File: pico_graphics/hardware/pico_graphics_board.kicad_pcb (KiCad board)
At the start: 2 copper layers, 99.1 x 86.4 mm, 28 parts, among them J1 8bit_thing_bus_connector, J2 HDMI_A, J3 greenpak_i2c, U1 Pico, U2 74LVC245, U3 74LVC245, U4 SLG46826G

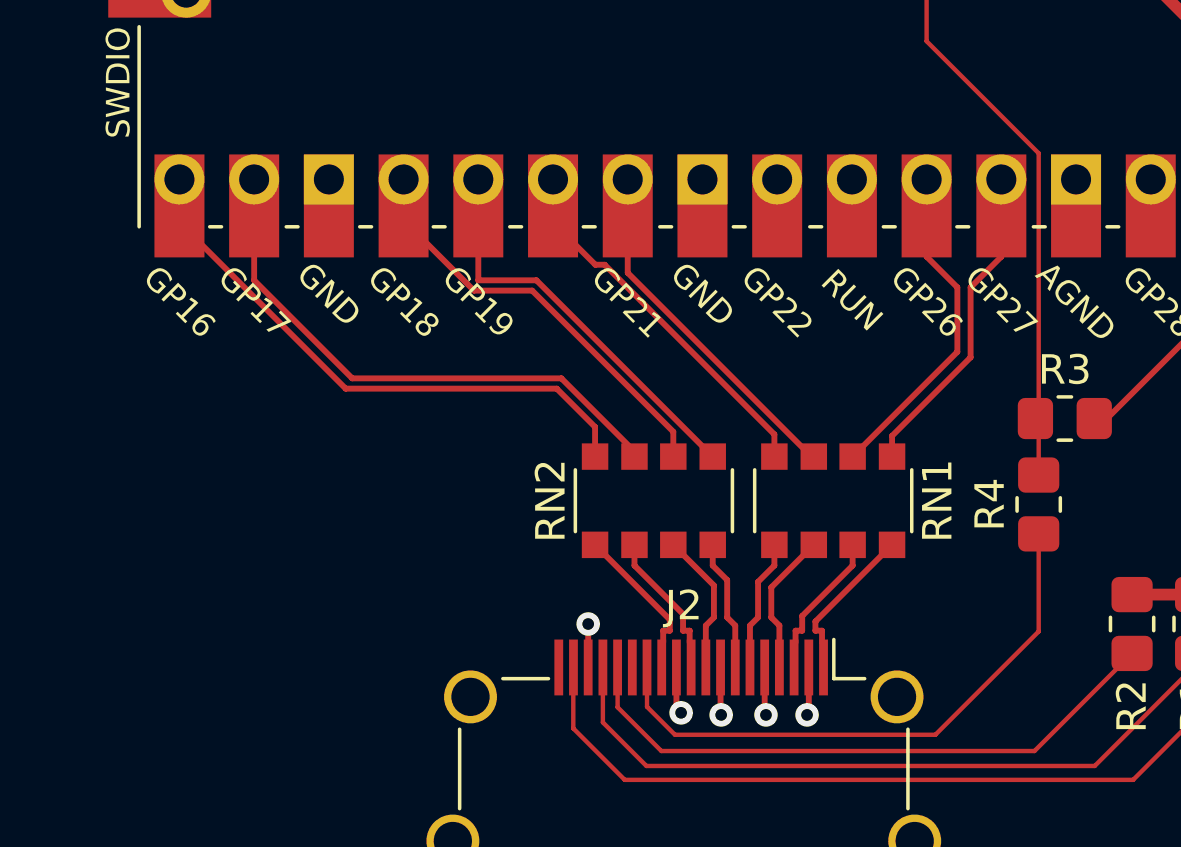
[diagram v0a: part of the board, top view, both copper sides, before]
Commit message: Fix resistor network footprint size
Kicad footprints are confusingly labeled by the individual resistor size as
opposed to the size of the full package - so 4x1206 means 'as big as 4x 1206
resistors' not as big as one 1206 as is used in manufacturers' datasheets.
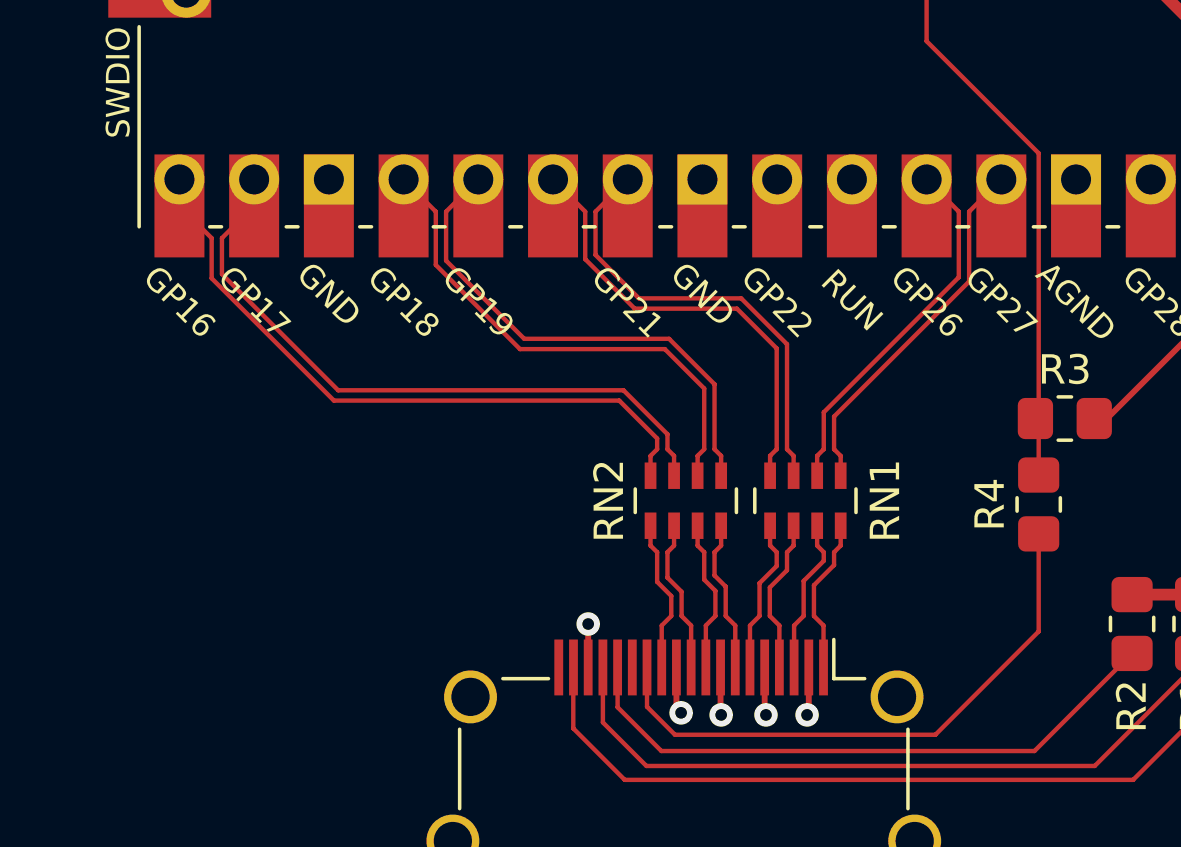
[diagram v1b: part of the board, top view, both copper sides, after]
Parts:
- RN1, RN2: footprint Resistor_SMD:R_Array_Convex_4x1206 -> Resistor_SMD:R_Array_Concave_4x0603
- moved RN2 1.09 mm to (107.8, 108.2)
- moved RN1 0.95 mm to (111.8, 108.2)
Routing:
- net /P_DVI_CK-: track 18.0 -> 22.6 mm
- net /P_DVI_D0-: track 13.0 -> 17.3 mm
- net /P_DVI_D1-: track 11.3 -> 15.4 mm
- net /P_DVI_CK+: track 18.8 -> 22.6 mm
- net /P_DVI_D0+: track 13.9 -> 17.3 mm
- net /P_DVI_D1+: track 12.0 -> 15.4 mm
- net /P_DVI_D2+: track 11.0 -> 12.5 mm
- net /P_DVI_D2-: track 11.3 -> 12.5 mm
- net /D2-: track 4.25 -> 5.33 mm
- net /CK+: track 4.23 -> 5.24 mm
- net /D1-: track 4.51 -> 5.29 mm
- net /D0+: track 4.49 -> 5.20 mm
- net /D2+: track 4.62 -> 5.33 mm
- net /CK-: track 4.60 -> 5.24 mm
